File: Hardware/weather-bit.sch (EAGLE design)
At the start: 39 parts, among them J10 SMD, J2 RJ11, J3 RJ11, J8 Qwiic (vertical), J9 SMD, U1 BME280, U2 micro:bit

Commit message: run of checklist
- vector font in sch
- added testpoints
- corrected measures
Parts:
- added TP1, TP13, TP14, TP19, TP2, TP3, TP4, TP5, TP8, TP9: TEST-POINTTP_15TH_THRU, SparkFun-Connectors:TEST-POINTTP_15TH_THRU
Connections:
- removed net 10: U2.P10
- removed net 11: U2.P11
- removed net 3: U2.P3
- removed net 4: U2.P4
- removed net 5: U2.P5
- removed net 6: U2.P6
- removed net 7: U2.P7
- removed net 9: U2.P9
- removed net N$3: U2.P13
- net 3.3V: now also TP1.1
- net GND: now also TP2.1
- net RAIN: now also TP8.1
- net SCL: now also TP4.1
- net SDA: now also TP3.1
- net SOIL_DAT: now also TP19.1
- net SOIL_PWR: now also TP5.1
- net TEMP_DAT: now also TP9.1
- net WDIR: now also TP14.1
- net WSPEED: now also TP13.1
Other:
- note added: "Testpoints"
- note added: "VCC RANGE: 3.3V Only to Micro:bit"
- moved on the sheet: U2

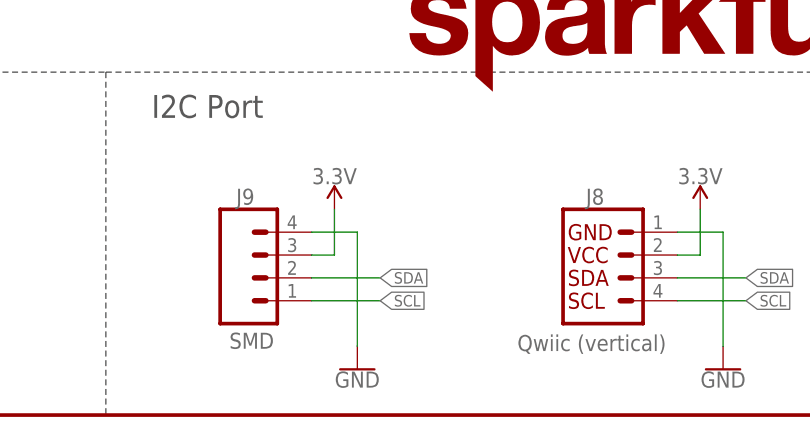
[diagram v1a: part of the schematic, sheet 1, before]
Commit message: switched to TIGHT DRC, nudging and routing
-updated package on 4-pin SMD to allow for routing to either pad under each header
-moved to TIGHT DRC, some slight nudging of routes to comply
-rotated SERIAL PORT silk to match pin labels
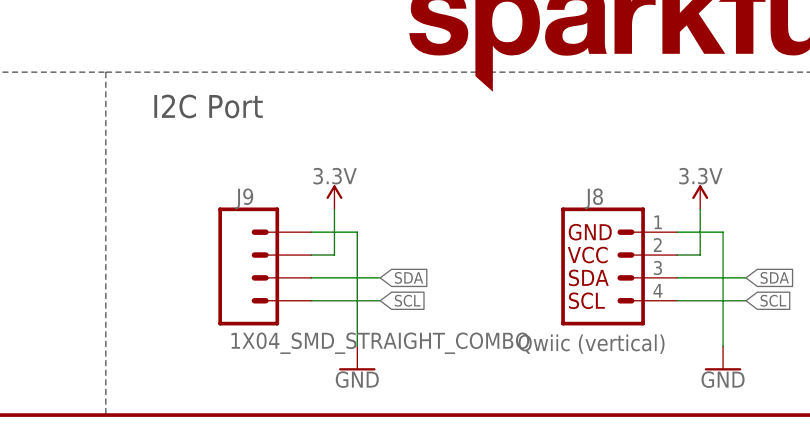
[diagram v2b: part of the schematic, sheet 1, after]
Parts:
- J9: value SMD -> 1X04_SMD_STRAIGHT_COMBO
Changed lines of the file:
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@@
 <grid distance="0.1" unitdist="inch" unit="inch" style="lines" multiple="1" display="no" altdistance="0.01" altunitdist="inch" altunit="inch"/>
 <layers>
-<layer number="1" name="Top" color="4" fill="1" visible="yes" active="no"/>
-<layer number="2" name="Route2" color="1" fill="3" visible="yes" active="no"/>
-<layer number="3" name="Route3" color="4" fill="3" visible="yes" active="no"/>
-<layer number="4" name="Route4" color="1" fill="4" visible="yes" active="no"/>
-<layer number="5" name="Route5" color="4" fill="4" visible="yes" active="no"/>
-<layer number="6" name="Route6" color="1" fill="8" visible="yes" active="no"/>
-<layer number="7" name="Route7" color="4" fill="8" visible="yes" active="no"/>
-<layer number="8" name="Route8" color="1" fill="2" visible="yes" active="no"/>
-<layer number="9" name="Route9" color="4" fill="2" visible="yes" active="no"/>
-<layer number="10" name="Route10" color="1" fill="7" visible="yes" active="no"/>
-<layer number="11" name="Route11" color="4" fill="7" visible="yes" active="no"/>
-<layer number="12" name="Route12" color="1" fill="5" visible="yes" active="no"/>
-<layer number="13" name="Route13" color="4" fill="5" visible="yes" active="no"/>
-<layer number="14" name="Route14" color="1" fill="6" visible="yes" active="no"/>
-<layer number="15" name="Route15" color="4" fill="6" visible="yes" active="no"/>
-<layer number="16" name="Bottom" color="1" fill="1" visible="yes" active="no"/>
-<layer number="17" name="Pads" color="2" fill="1" visible="yes" active="no"/>
-<layer number="18" name="Vias" color="2" fill="1" visible="yes" active="no"/>
-<layer number="19" name="Unrouted" color="6" fill="1" visible="yes" active="no"/>
-<layer number="20" name="Dimension" color="15" fill="1" visible="yes" active="no"/>
-<layer number="21" name="tPlace" color="16" fill="1" visible="yes" active="no"/>
-<layer number="22" name="bPlace" color="14" fill="1" visible="yes" active="no"/>
-<layer number="23" name="tOrigins" color="15" fill="1" visible="yes" active="no"/>
-<layer number="24" name="bOrigins" color="15" fill="1" visible="yes" active="no"/>
-<layer number="25" name="tNames" color="7" fill="1" visible="yes" active="no"/>
-<layer number="26" name="bNames" color="7" fill="1" visible="yes" active="no"/>
-<layer number="27" name="tValues" color="7" fill="1" visible="yes" active="no"/>
-<layer number="28" name="bValues" color="7" fill="1" visible="yes" active="no"/>
+<layer number="1" name="Top" color="4" fill="1" visible="no" active="no"/>
+<layer number="2" name="Route2" color="1" fill="3" visible="no" active="no"/>
+<layer number="3" name="Route3" color="4" fill="3" visible="no" active="no"/>
+<layer number="4" name="Route4" color="1" fill="4" visible="no" active="no"/>
+<layer number="5" name="Route5" color="4" fill="4" visible="no" active="no"/>
+<layer number="6" name="Route6" color="1" fill="8" visible="no" active="no"/>
+<layer number="7" name="Route7" color="4" fill="8" visible="no" active="no"/>
+<layer number="8" name="Route8" color="1" fill="2" visible="no" active="no"/>
+<layer number="9" name="Route9" color="4" fill="2" visible="no" active="no"/>
+<layer number="10" name="Route10" color="1" fill="7" visible="no" active="no"/>
+<layer number="11" name="Route11" color="4" fill="7" visible="no" active="no"/>
+<layer number="12" name="Route12" color="1" fill="5" visible="no" active="no"/>
+<layer number="13" name="Route13" color="4" fill="5" visible="no" active="no"/>
+<layer number="14" name="Route14" color="1" fill="6" visible="no" active="no"/>
+<layer number="15" name="Route15" color="4" fill="6" visible="no" active="no"/>
+<layer number="16" name="Bottom" color="1" fill="1" visible="no" active="no"/>
+<layer number="17" name="Pads" color="2" fill="1" visible="no" active="no"/>
+<layer number="18" name="Vias" color="2" fill="1" visible="no" active="no"/>
+<layer number="19" name="Unrouted" color="6" fill="1" visible="no" active="no"/>
+<layer number="20" name="Dimension" color="15" fill="1" visible="no" active="no"/>
+<layer number="21" name="tPlace" color="16" fill="1" visible="no" active="no"/>
+<layer number="22" name="bPlace" color="14" fill="1" visible="no" active="no"/>
+<layer number="23" name="tOrigins" color="15" fill="1" visible="no" active="no"/>
+<layer number="24" name="bOrigins" color="15" fill="1" visible="no" active="no"/>
+<layer number="25" name="tNames" color="7" fill="1" visible="no" active="no"/>
+<layer number="26" name="bNames" color="7" fill="1" visible="no" active="no"/>
+<layer number="27" name="tValues" color="7" fill="1" visible="no" active="no"/>
+<layer number="28" name="bValues" color="7" fill="1" visible="no" active="no"/>
 <layer number="29" name="tStop" color="7" fill="3" visible="no" active="no"/>
 <layer number="30" name="bStop" color="7" fill="6" visible="no" active="no"/>
@@
 <layer number="35" name="tGlue" color="7" fill="4" visible="no" active="no"/>
 <layer number="36" name="bGlue" color="7" fill="5" visible="no" active="no"/>
-<layer number="37" name="tTest" color="7" fill="1" visible="yes" active="no"/>
-<layer number="38" name="bTest" color="7" fill="1" visible="yes" active="no"/>
+<layer number="37" name="tTest" color="7" fill="1" visible="no" active="no"/>
+<layer number="38" name="bTest" color="7" fill="1" visible="no" active="no"/>
 <layer number="39" name="tKeepout" color="4" fill="11" visible="no" active="no"/>
 <layer number="40" name="bKeepout" color="1" fill="11" visible="no" active="no"/>
@@
 <layer number="44" name="Drills" color="7" fill="1" visible="no" active="no"/>
 <layer number="45" name="Holes" color="7" fill="1" visible="no" active="no"/>
-<layer number="46" name="Milling" color="3" fill="1" visible="yes" active="no"/>
-<layer number="47" name="Measures" color="7" fill="1" visible="yes" active="no"/>
-<layer number="48" name="Document" color="7" fill="1" visible="yes" active="no"/>
-<layer number="49" name="Reference" color="7" fill="1" visible="yes" active="no"/>
-<layer number="50" name="dxf" color="7" fill="1" visible="yes" active="no"/>
-<layer number="51" name="tDocu" color="6" fill="1" visible="yes" active="no"/>
-<layer number="52" name="bDocu" color="7" fill="1" visible="yes" active="no"/>
-<layer number="53" name="tGND_GNDA" color="7" fill="9" visible="yes" active="no"/>
-<layer number="54" name="bGND_GNDA" color="1" fill="9" visible="yes" active="no"/>
-<layer number="56" name="wert" color="7" fill="1" visible="yes" active="no"/>
-<layer number="57" name="tCAD" color="7" fill="1" visible="yes" active="no"/>
-<layer number="59" name="tCarbon" color="7" fill="1" visible="yes" active="no"/>
-<layer number="60" name="bCarbon" color="7" fill="1" visible="yes" active="no"/>
+<layer number="46" name="Milling" color="3" fill="1" visible="no" active="no"/>
+<layer number="47" name="Measures" color="7" fill="1" visible="no" active="no"/>
+<layer number="48" name="Document" color="7" fill="1" visible="no" active="no"/>
+<layer number="49" name="Reference" color="7" fill="1" visible="no" active="no"/>
+<layer number="50" name="dxf" color="7" fill="1" visible="no" active="no"/>
+<layer number="51" name="tDocu" color="6" fill="1" visible="no" active="no"/>
+<layer number="52" name="bDocu" color="7" fill="1" visible="no" active="no"/>
+<layer number="53" name="tGND_GNDA" color="7" fill="9" visible="no" active="no"/>
+<layer number="54" name="bGND_GNDA" color="1" fill="9" visible="no" active="no"/>
+<layer number="56" name="wert" color="7" fill="1" visible="no" active="no"/>
+<layer number="57" name="tCAD" color="7" fill="1" visible="no" active="no"/>
+<layer number="59" name="tCarbon" color="7" fill="1" visible="no" active="no"/>
+<layer number="60" name="bCarbon" color="7" fill="1" visible="no" active="no"/>
 <layer number="88" name="SimResults" color="9" fill="1" visible="no" active="yes"/>
 <layer number="89" name="SimProbes" color="9" fill="1" visible="no" active="yes"/>
@@
 <part name="SUPPLY9" library="SparkFun-PowerSymbols" deviceset="3.3V" device=""/>
 <part name="SUPPLY10" library="SparkFun-PowerSymbols" deviceset="3.3V" device=""/>
-<part name="J9" library="SparkFun-Connectors" deviceset="CONN_04" device="SMD_STRAIGHT_COMBO" value="SMD"/>
+<part name="J9" library="SparkFun-Connectors" deviceset="CONN_04" device="SMD_STRAIGHT_COMBO" value="1X04_SMD_STRAIGHT_COMBO"/>
 <part name="SUPPLY11" library="SparkFun-PowerSymbols" deviceset="3.3V" device=""/>
 <part name="GND2" library="SparkFun-PowerSymbols" deviceset="GND" device=""/>

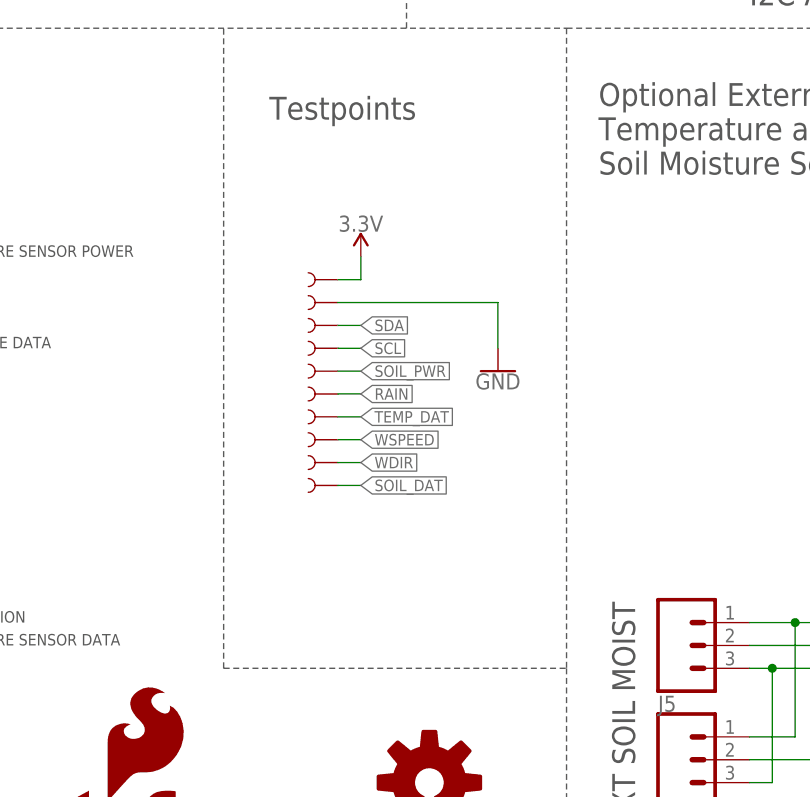
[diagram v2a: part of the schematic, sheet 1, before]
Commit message: Finalized test points and test point positions
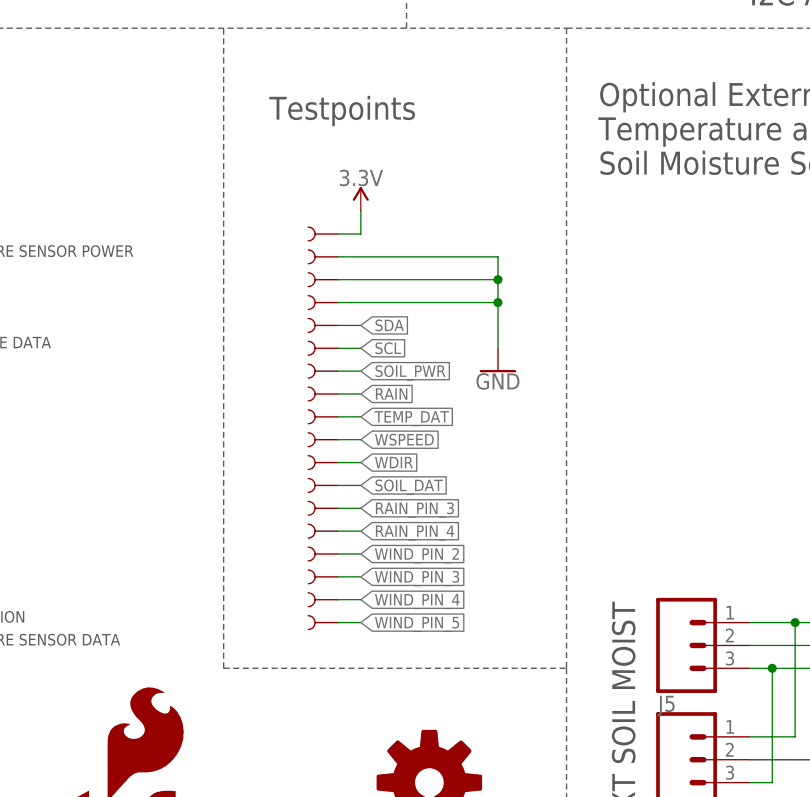
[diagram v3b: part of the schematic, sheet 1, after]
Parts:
- added TP10, TP11, TP12, TP15, TP6, TP7: TEST-POINT3X4, SparkFun-Connectors:TEST-POINT3X4
- added TP16, TP17: TEST-POINTTP_15TH_THRU, SparkFun-Connectors:TEST-POINTTP_15TH_THRU
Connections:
- removed net N$11: J3.3, R9.2
- removed net N$13: J3.5, R6.2
- removed net N$14: J3.4, R7.2
- removed net N$5: J2.3, R4.1
- removed net N$6: J3.2, R8.2
- removed net N$7: J2.4, R5.2
- new net RAIN_PIN_3: J2.3, R4.1, TP6.1
- new net RAIN_PIN_4: J2.4, R5.2, TP7.1
- new net WIND_PIN_2: J3.2, R8.2, TP10.1
- new net WIND_PIN_3: J3.3, R9.2, TP11.1
- new net WIND_PIN_4: J3.4, R7.2, TP12.1
- new net WIND_PIN_5: J3.5, R6.2, TP15.1
- net GND: now also TP16.1, TP17.1
